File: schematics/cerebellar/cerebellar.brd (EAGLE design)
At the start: 98.4 x 91.1 mm, 64 parts, among them CON2 ODrive1, CON4 Odrive3, CON5 ODrive4, CON6 Odrive2, CON7 ODrive5, CON8 ODrive6, IC3 LTC7001, P1 Foot1, P10 SPI2, P11 Foot2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

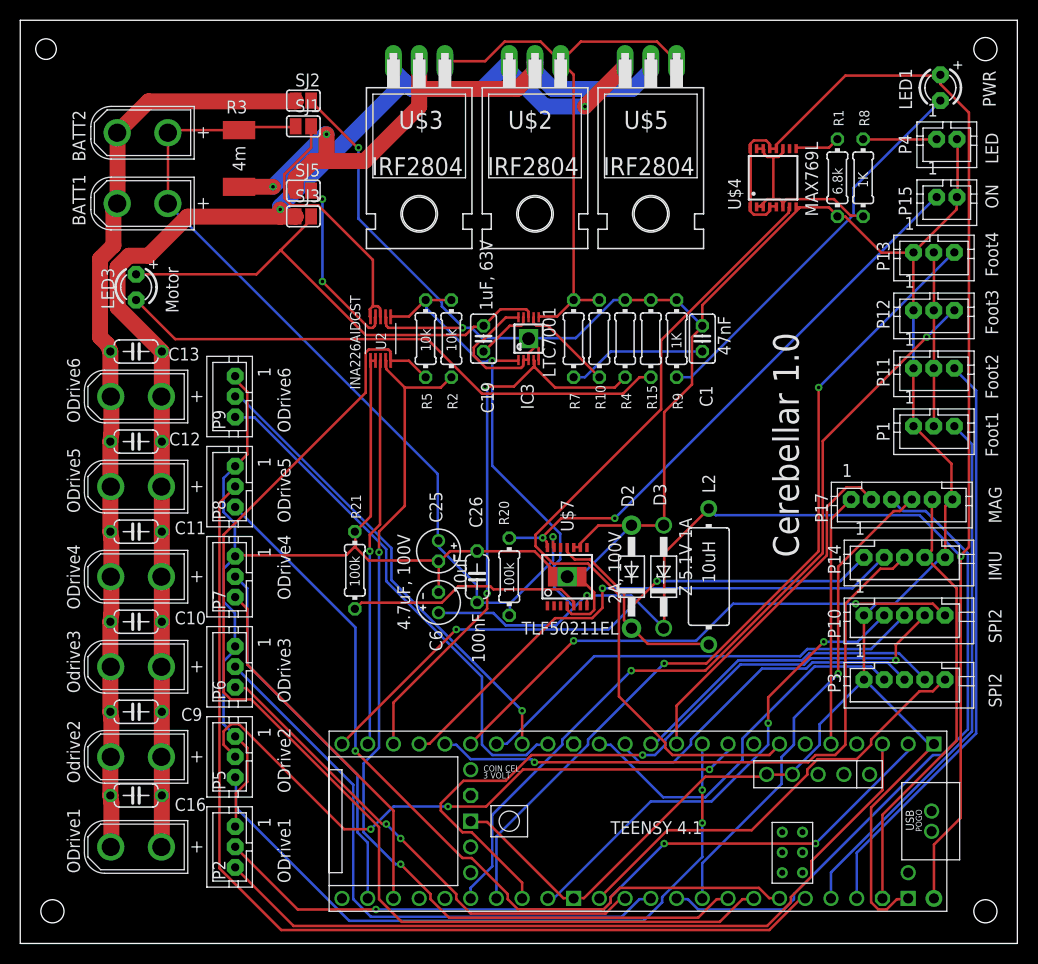
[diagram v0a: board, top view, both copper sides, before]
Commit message: added Magnetometer to UKF
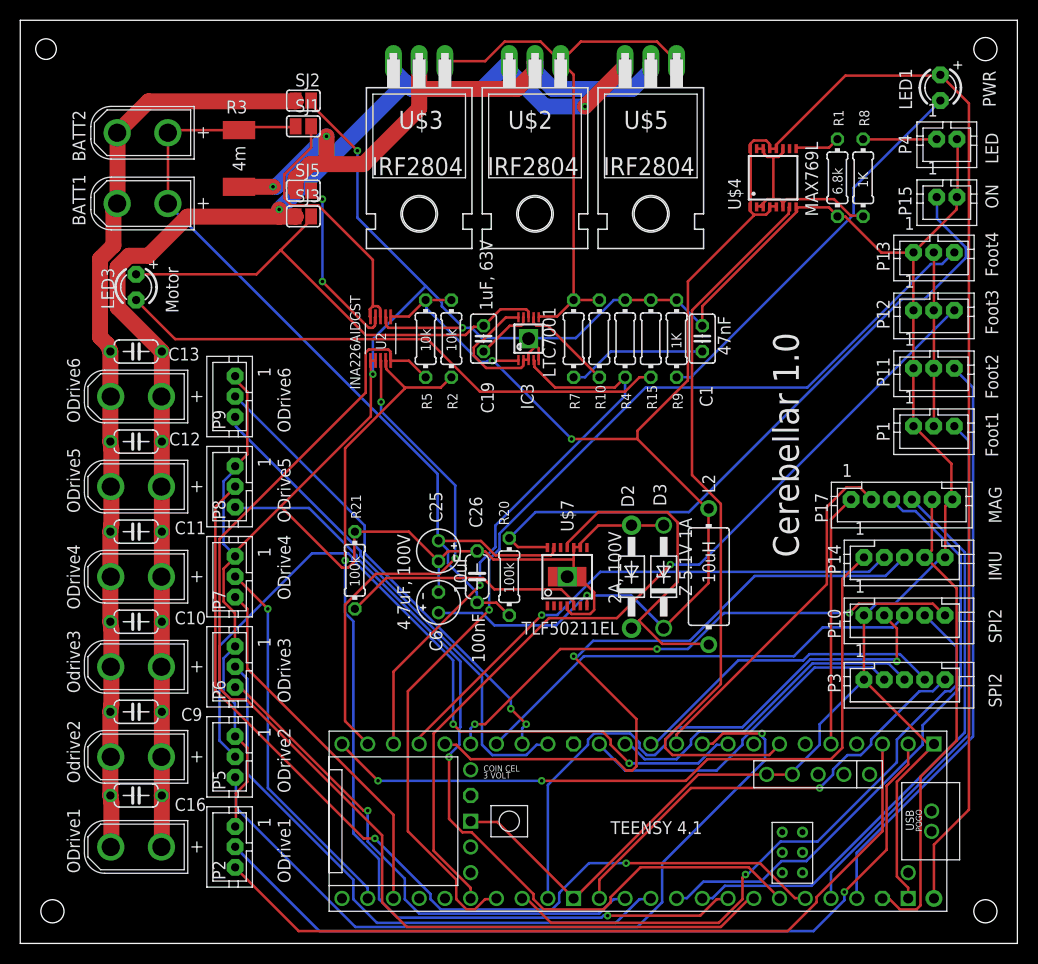
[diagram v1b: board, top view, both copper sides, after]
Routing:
- net SENS4: track 84.9 -> 103.1 mm, vias 2 -> 1
- net O2_RX: track 61.2 -> 79.1 mm, vias 3 -> 2
- net N$42: track 19.8 -> 33.2 mm
- net GND: track 413.2 -> 399.8 mm, vias 2 -> 3
- net IMU_ENABLE: track 59.2 -> 72.0 mm, vias 3 -> 2
- net N$5: track 38.4 -> 50.0 mm, vias 1 -> 2
- net MISO1: track 47.5 -> 58.6 mm, vias 2 -> 1
- net O2_TX: track 67.7 -> 78.3 mm, vias 2 -> 1
- net N$47: track 57.3 -> 67.9 mm, vias 2 -> 0
- net LED_PWM: track 83.2 -> 72.9 mm
- net MAG_SDA: track 48.3 -> 57.9 mm, vias 1 -> 0
- net O5_RX: track 100.0 -> 92.3 mm, vias 0 -> 2
- net T_RX: track 62.7 -> 70.3 mm
- net O1_RX: track 76.5 -> 82.9 mm, vias 3 -> 1
- net CS1: track 70.1 -> 64.4 mm, vias 2 -> 1
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
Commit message: added 3.3V power supply
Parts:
- added C2: 100nF, rcl:C025-025X050
- added C4: 2.2uF, rcl:C025-025X050
- added U$6: MAX884, MAX884:SO08
- moved LED3 9.55 mm to (14.6, 65.4)
- moved U$3 1.91 mm to (31.1, 79.4)
- moved U$2 1.91 mm to (42.5, 79.4)
- moved U$5 1.91 mm to (54.0, 79.4)
- moved BATT1 0.63 mm to (5.08, 73.0)
- moved BATT2 0.63 mm to (5.08, 80.0)
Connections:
- removed net UC3.3V: P14.4, P17.5, U$1.3V3-3
- new net N$7: U$1.3V3-3
- net +3.3V: now also C4.1, P14.4, P17.5, U$6.4
- net +5V: now also C2.1, U$6.5, U$6.8
- net BATT+: no longer C25.+, C26.1, R20.1, U$7.13
- net GND: now also C2.2, C4.2, U$6.2, U$6.3, U$6.6
- net V+: now also C25.+, C26.1, R20.1, U$7.13
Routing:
- net BATT+: track 88.3 -> 20.6 mm
- net V+: track 26.9 -> 87.2 mm, vias 0 -> 1
- net UC3.3V: track 47.6 -> 0.00 mm
- net O2_TX: track 78.3 -> 47.5 mm
- net +3.3V: track 17.2 -> 45.6 mm
- net O2_RX: track 79.1 -> 51.2 mm, vias 2 -> 1
- net +5V: track 229.9 -> 255.5 mm, vias 3 -> 2
- net GND: track 399.8 -> 424.2 mm, vias 3 -> 1
- net N$10: track 56.6 -> 76.5 mm, vias 1 -> 0
- net T_RX: track 70.3 -> 53.0 mm
- net N$26: track 49.5 -> 37.4 mm, vias 0 -> 1
- net IMU_ENABLE: track 72.0 -> 60.4 mm
- net O3_TX: track 51.4 -> 62.7 mm, vias 1 -> 0
- net SENS4: track 103.1 -> 91.8 mm
- net MISO1: track 58.6 -> 47.4 mm
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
